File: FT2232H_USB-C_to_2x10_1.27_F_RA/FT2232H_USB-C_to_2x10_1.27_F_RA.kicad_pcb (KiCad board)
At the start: 4 copper layers, 39.8 x 60 mm, 42 parts, among them J1 USB_B_Micro, J2 Conn_02x10_Odd_Even, J3 Conn_02x10_Odd_Even, U1 FT2232HL, U2 93C46BT-I_OT, U3 USBLC6-2SC6, U4 MIC5504-3.3YM5, X1 DSC60xx

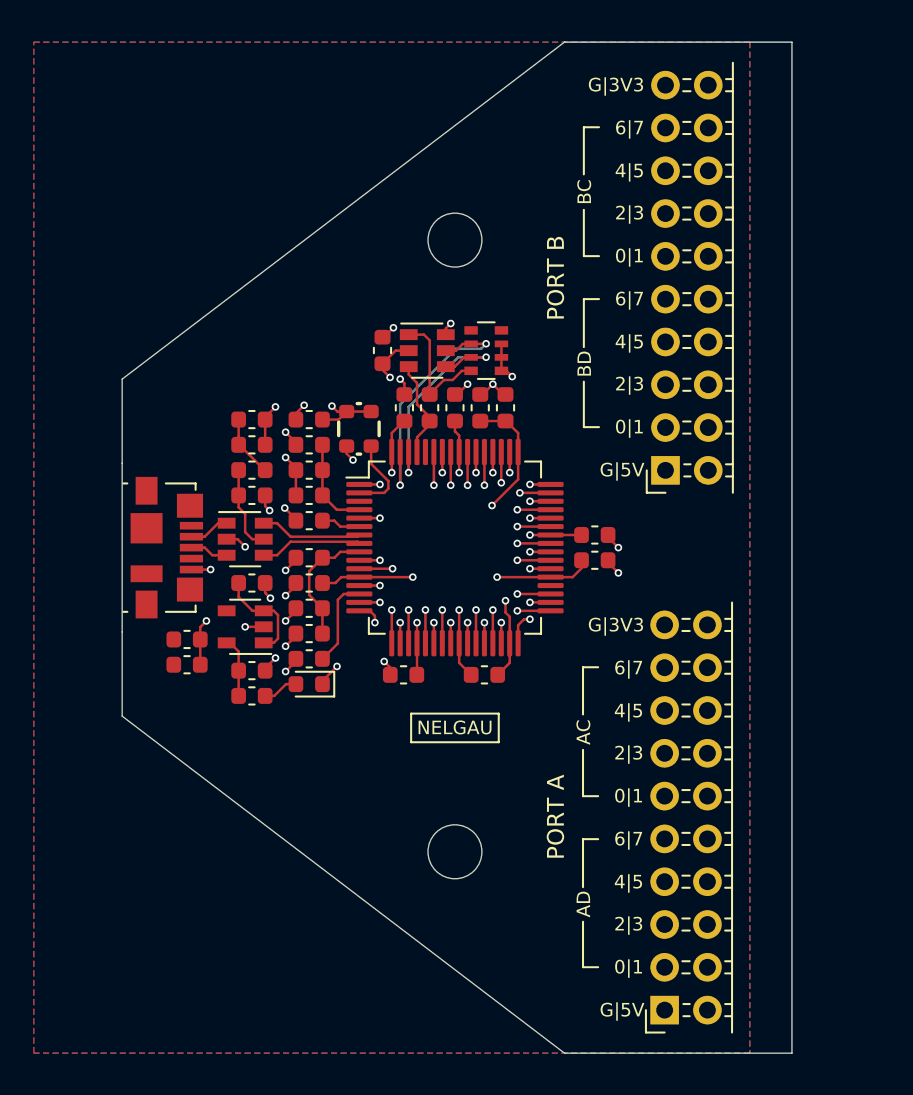
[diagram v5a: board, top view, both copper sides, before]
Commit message: Clean up layout around FT2232H
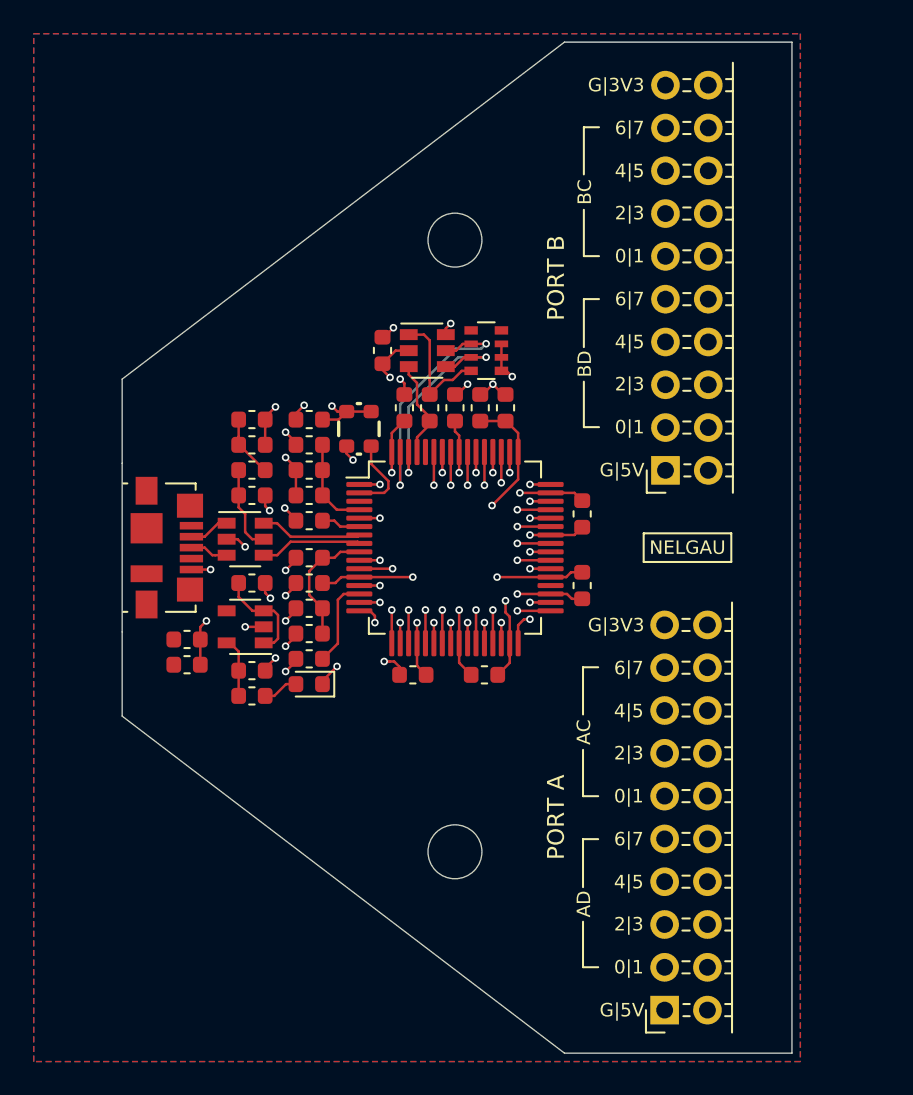
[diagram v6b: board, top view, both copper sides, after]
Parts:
- moved SYM1 17.5 mm to (174.8, 97.0)
- moved C16 1.68 mm to (168.6, 99.3), turned to 270 degrees
- moved C11 1.46 mm to (168.6, 95.0), turned to 90 degrees
- moved C9 0.55 mm to (158.5, 104.6)
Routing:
- net GND: track 49.6 -> 52.2 mm, vias 33 -> 31
- net P1V8: track 22.1 -> 21.6 mm

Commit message: Rough routing of data and control output buses
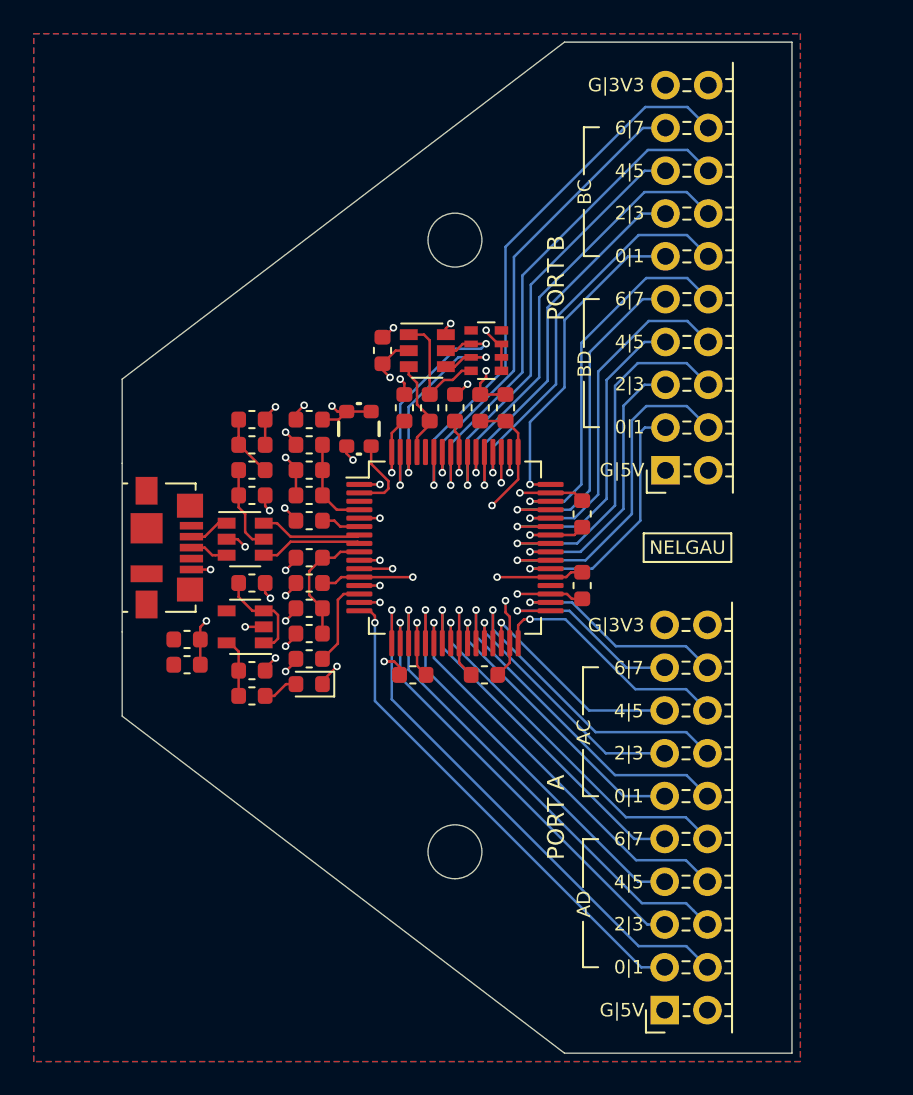
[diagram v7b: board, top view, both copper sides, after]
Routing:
- net /BC7: track 1.98 -> 33.9 mm
- net /AD1: track 1.98 -> 32.6 mm
- net /BC5: track 1.98 -> 30.8 mm
- net /AD0: track 1.45 -> 29.8 mm
- net /AD3: track 1.98 -> 29.5 mm
- net /BC6: track 1.23 -> 28.0 mm
- net /BC3: track 1.23 -> 26.3 mm
- net /AD2: track 1.23 -> 26.2 mm
- net /BC4: track 1.98 -> 26.2 mm
- net /AD5: track 1.23 -> 25.1 mm
- net /AD4: track 1.98 -> 24.9 mm
- net /BC1: track 1.23 -> 23.6 mm
- net /BD7: track 1.23 -> 22.7 mm
- net /BC2: track 1.98 -> 23.4 mm
- net /AD7: track 1.23 -> 22.4 mm
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
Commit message: Finish routing data and control buses
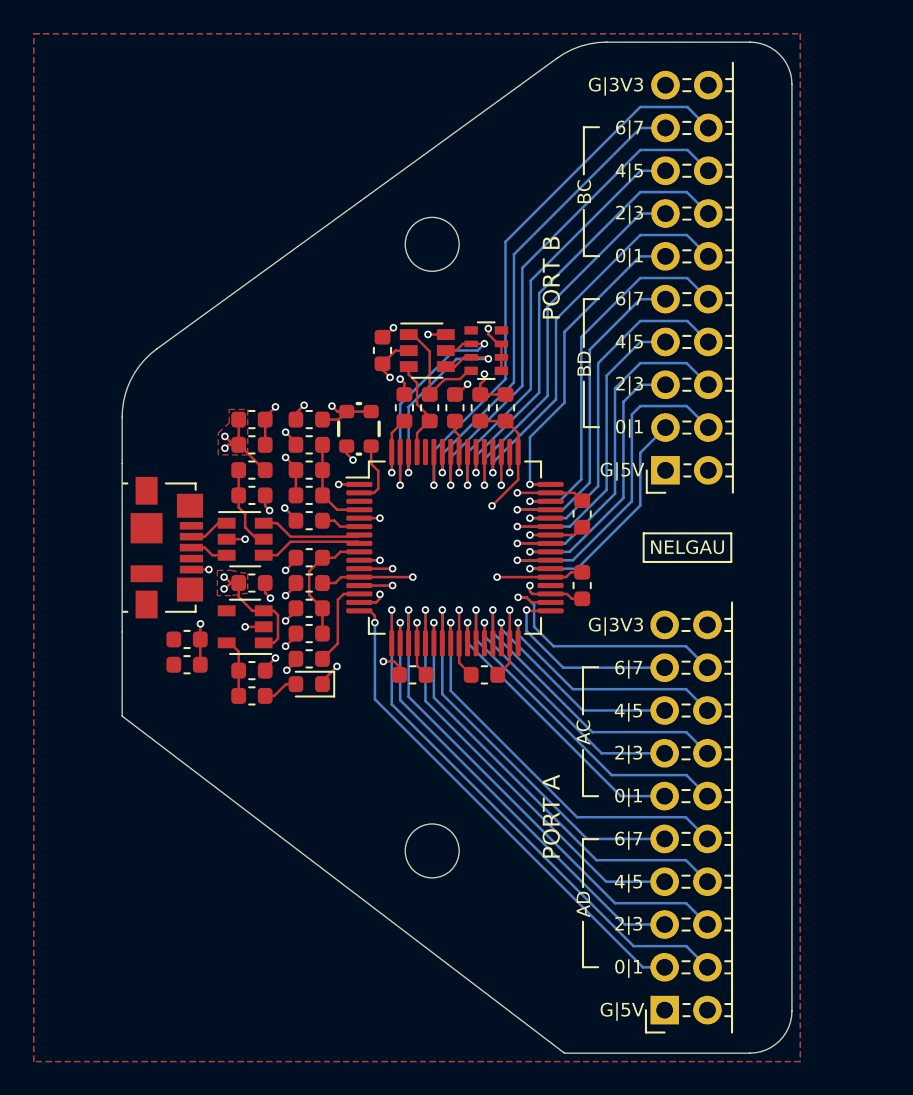
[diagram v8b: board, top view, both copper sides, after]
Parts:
- moved H2 1.37 mm to (159.7, 79.0)
- moved H1 1.35 mm to (159.7, 115.0)
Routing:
- net USB_5V: track 9.66 -> 102.7 mm, vias 0 -> 4
- net /AC7: track 13.4 -> 15.8 mm
- net /AD7: track 22.4 -> 24.1 mm
- net /AD6: track 22.1 -> 23.7 mm
- net /AD5: track 25.1 -> 26.4 mm
- net /BD0: track 15.8 -> 14.6 mm
- net /AD4: track 24.9 -> 26.0 mm
- net /AD3: track 29.5 -> 30.5 mm
- net /USB_OSC: track 4.78 -> 3.93 mm
- net /AD2: track 26.2 -> 27.0 mm
- added copper zone on F.Cu, net USB_5V
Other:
- outline, holes or cut-outs redrawn
